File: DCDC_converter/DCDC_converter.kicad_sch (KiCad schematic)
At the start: 30 parts, among them J24 Conn_01x02, U10 MP2491C, U11 AMS1117-3.3, U14 MIC2026-1xM, U15 MIC2026-1xM, U17 MIC2026-1xM, U9 MP2491C

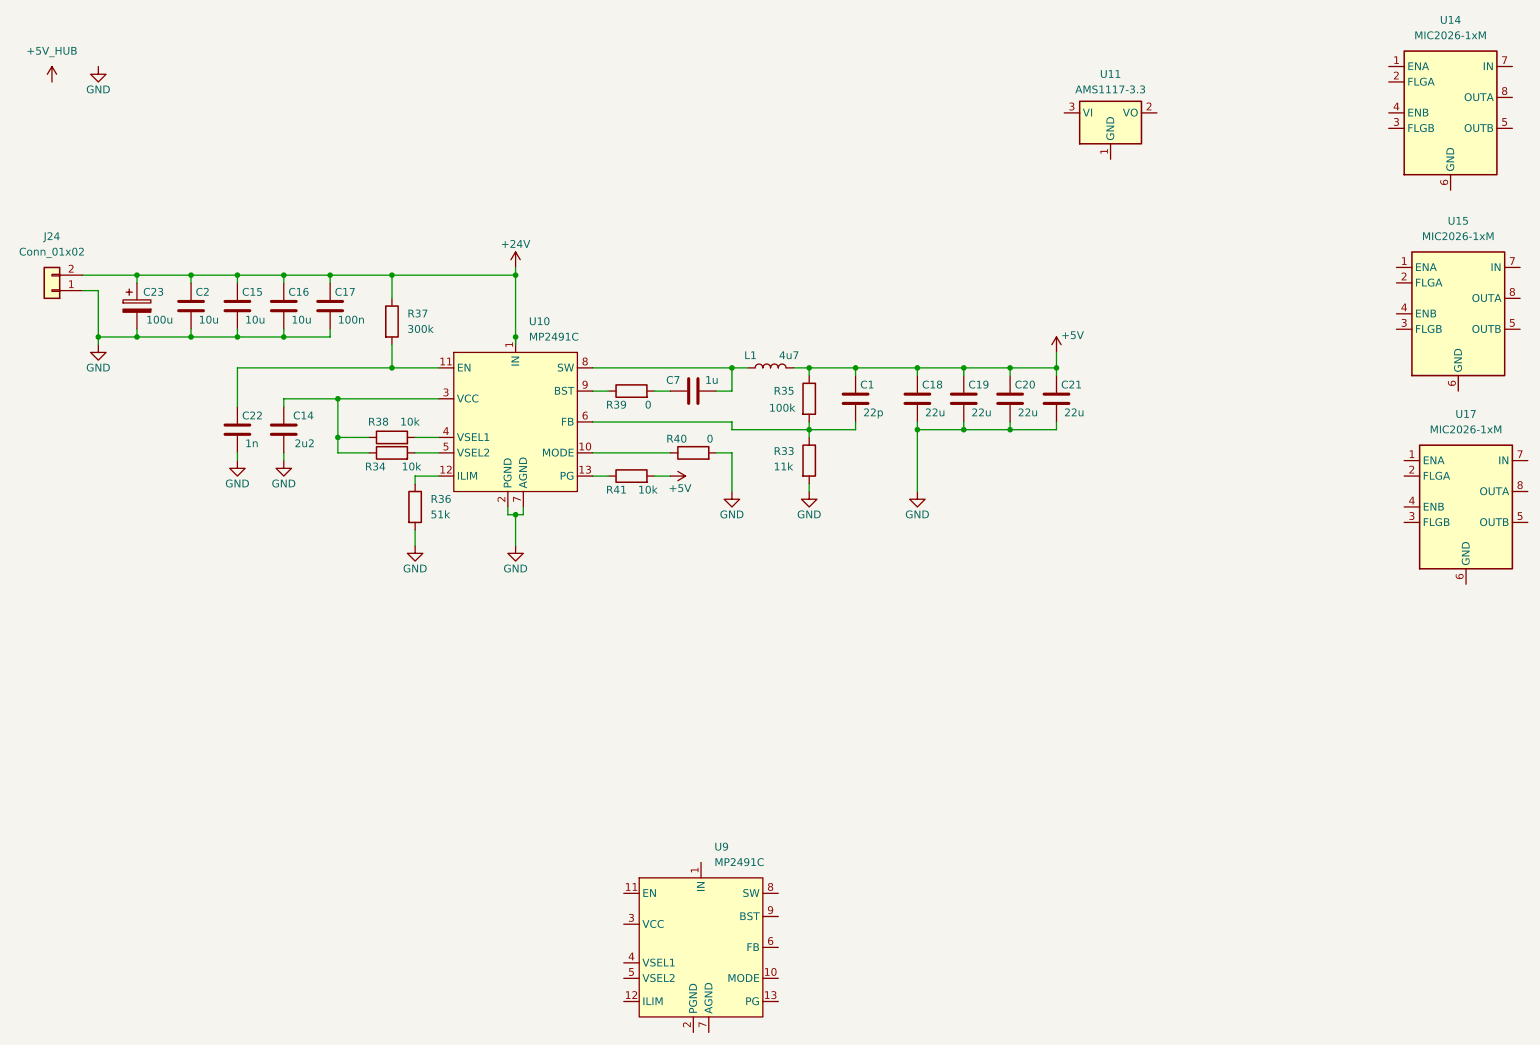
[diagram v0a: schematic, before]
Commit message: Made custom solo PCB for DC/DC converter
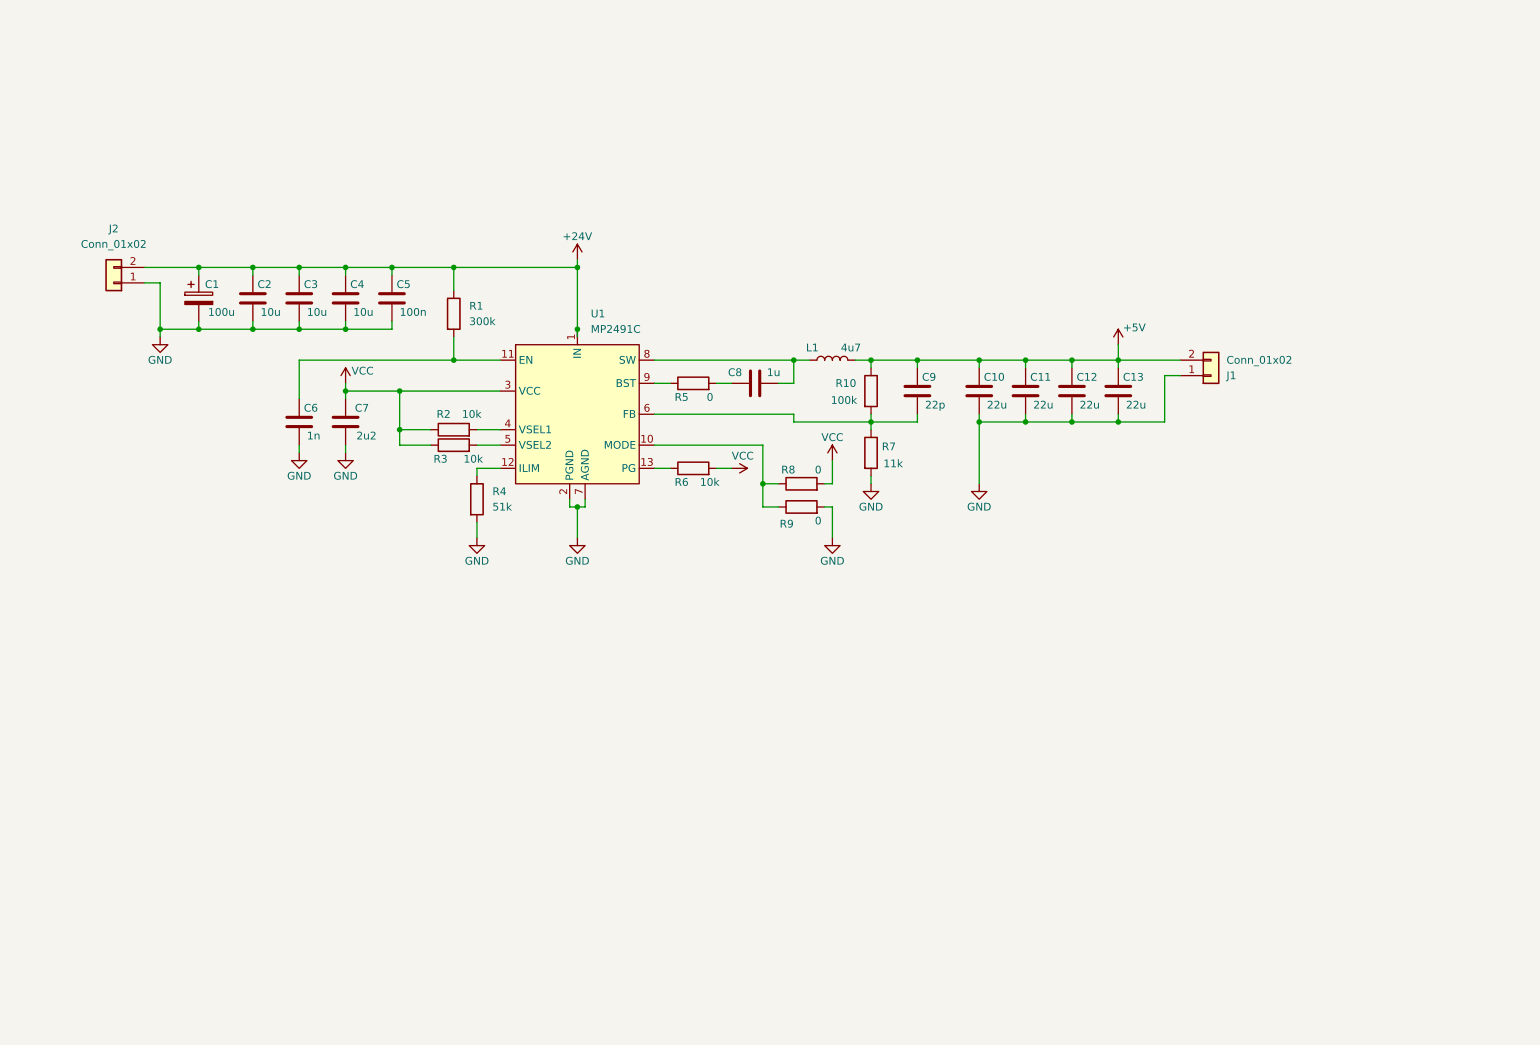
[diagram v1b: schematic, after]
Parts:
- removed C1: 22p, symbol Device:C
- removed C14: 2u2, symbol Device:C
- removed C15, C16: 10u, symbol Device:C
- removed C17: 100n, symbol Device:C
- removed C18, C19, C20, C21: 22u, symbol Device:C
- removed C22: 1n, symbol Device:C
- removed C23: 100u, symbol Device:C_Polarized
- removed J24: Conn_01x02, Connector_Phoenix_MSTB:PhoenixContact_MSTBA_2,5_2-G_1x02_P5.00mm_Horizontal, symbol Connector_Generic:Conn_01x02
- removed R33: 11k, symbol Device:R
- removed R34, R38, R41: 10k, symbol Device:R
- removed R35: 100k, symbol Device:R
- removed R36: 51k, symbol Device:R
- removed R37: 300k, symbol Device:R
- removed R39, R40: 0, symbol Device:R
- removed U10, U9: MP2491C, HK:QFN-13_HK, symbol HK:MP2491C_HK
- removed U11: AMS1117-3.3, Package_TO_SOT_SMD:SOT-223-3_TabPin2, symbol Regulator_Linear:AMS1117-3.3
- removed U14, U15, U17: MIC2026-1xM, Package_SO:SOIC-8_3.9x4.9mm_P1.27mm, symbol Power_Management:MIC2026-1xM
- added C1: 100u, Capacitor_THT:CP_Radial_D6.3mm_P2.50mm, symbol Device:C_Polarized
- added C10, C11, C12, C13: 22u, Capacitor_SMD:C_0805_2012Metric, symbol Device:C
- added C3, C4: 10u, Capacitor_SMD:C_0805_2012Metric, symbol Device:C
- added C5: 100n, Capacitor_SMD:C_0603_1608Metric, symbol Device:C
- added C6: 1n, Capacitor_SMD:C_0603_1608Metric, symbol Device:C
- added C8: 1u, Capacitor_SMD:C_0603_1608Metric, symbol Device:C
- added C9: 22p, Capacitor_SMD:C_0603_1608Metric, symbol Device:C
- added J1, J2: Conn_01x02, Connector_Phoenix_MSTB:PhoenixContact_MSTBA_2,5_2-G_1x02_P5.00mm_Horizontal, symbol Connector_Generic:Conn_01x02
- added R1: 300k, Resistor_SMD:R_0603_1608Metric, symbol Device:R
- added R10: 100k, Resistor_SMD:R_0603_1608Metric, symbol Device:R
- added R2, R3, R6: 10k, Resistor_SMD:R_0603_1608Metric, symbol Device:R
- added R4: 51k, Resistor_SMD:R_0603_1608Metric, symbol Device:R
- added R5, R8, R9: 0, Resistor_SMD:R_0603_1608Metric, symbol Device:R
- added R7: 11k, Resistor_SMD:R_0603_1608Metric, symbol Device:R
- added U1: MP2491C, HK:QFN-13_HK, symbol HK:MP2491C_HK
- C2: footprint (none) -> Capacitor_SMD:C_0805_2012Metric
- C7: value 1u -> 2u2; footprint (none) -> Capacitor_SMD:C_0603_1608Metric
- L1: footprint (none) -> Inductor_SMD:L_Bourns-SRN8040_8x8.15mm
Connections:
- net +24V: now also C1.1, C3.1, C4.1, C5.1, J2.2 (Pin_2), R1.1, U1.1 (IN)
- net +5V: now also C10.1, C11.1, C12.1, C13.1, C9.1, J1.2 (Pin_2), R10.1
- net GND: now also C7.2, C1.2, C10.2, C11.2, C12.2, C13.2, C3.2, C4.2, C5.2, C6.2, J1.1 (Pin_1), J2.1 (Pin_1), R4.2, R7.2, R9.2, U1.2 (PGND), U1.7 (AGND)
- net at L1.1: now also C8.1, U1.8 (SW); no longer C7.1
- new net: R8.1, R9.1, U1.10 (MODE)
- new net: R2.2, U1.4 (VSEL1)
- new net: R4.1, U1.12 (ILIM)
- new net: C9.2, R10.2, R7.1, U1.6 (FB)
- new net: C6.1, R1.2, U1.11 (EN)
- new net: R6.1, U1.13 (PG)
- new net: R3.2, U1.5 (VSEL2)
- new net: R5.1, U1.9 (BST)
- new net: C8.2, R5.2
- new net VCC: C7.1, R2.1, R3.1, R6.2, R8.2, U1.3 (VCC)

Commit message: Last update
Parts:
- added D1: LED, symbol Device:LED
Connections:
- net +24V: now also J2.1 (Pin_1); no longer J2.2 (Pin_2)
- net GND: now also J2.2 (Pin_2); no longer J2.1 (Pin_1)
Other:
- moved on the sheet: J2
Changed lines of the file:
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@@
 	(wire
 		(pts
-			(xy 118.11 58.42) (xy 118.11 59.69)
+			(xy 118.11 57.15) (xy 118.11 59.69)
 		)
 		(stroke
@@
 	(symbol
 		(lib_id "Connector_Generic:Conn_01x02")
-		(at 41.91 62.23 180)
+		(at 41.91 59.69 0)
+		(mirror y)
 		(unit 1)
 		(exclude_from_sim no)
@@
 		(on_board yes)
 		(dnp no)
-		(fields_autoplaced yes)
 		(property "Reference" "J2"
-			(at 41.91 53.34 0)
+			(at 41.91 68.58 0)
 			(effects
 				(font
@@
 		)
 		(property "Value" "Conn_01x02"
-			(at 41.91 55.88 0)
+			(at 41.91 66.04 0)
 			(effects
 				(font
@@
 		)
 		(property "Footprint" "Connector_Phoenix_MSTB:PhoenixContact_MSTBA_2,5_2-G_1x02_P5.00mm_Horizontal"
-			(at 41.91 62.23 0)
+			(at 41.91 59.69 0)
 			(effects
 				(font
@@
 		)
 		(property "Datasheet" "~"
-			(at 41.91 62.23 0)
+			(at 41.91 59.69 0)
 			(effects
 				(font
@@
 		)
 		(property "Description" "Generic connector, single row, 01x02, script generated (kicad-library-utils/schlib/autogen/connector/)"
-			(at 41.91 62.23 0)
+			(at 41.91 59.69 0)
 			(effects
 				(font
@@
 	)
 	(symbol
+		(lib_id "Device:LED")
+		(at 139.7 105.41 90)
+		(unit 1)
+		(exclude_from_sim no)
+		(in_bom yes)
+		(on_board yes)
+		(dnp no)
+		(fields_autoplaced yes)
+		(property "Reference" "D1"
+			(at 143.51 105.7274 90)
+			(effects
+				(font
+					(size 1.27 1.27)
+				)
+				(justify right)
+			)
+		)
+		(property "Value" "LED"
+			(at 143.51 108.2674 90)
+			(effects
+				(font
+					(size 1.27 1.27)
+				)
+				(justify right)
+			)
+		)
+		(property "Footprint" ""
+			(at 139.7 105.41 0)
+			(effects
+				(font
+					(size 1.27 1.27)
+				)
+				(hide yes)
+			)
+		)
+		(property "Datasheet" "~"
+			(at 139.7 105.41 0)
+			(effects
+				(font
+					(size 1.27 1.27)
+				)
+				(hide yes)
+			)
+		)
+		(property "Description" "Light emitting diode"
+			(at 139.7 105.41 0)
+			(effects
+				(font
+					(size 1.27 1.27)
+				)
+				(hide yes)
+			)
+		)
+		(pin "2"
+		)
+		(pin "1"
+		)
+		(instances
+			(project ""
+				(path "/ace81164-188f-43a4-8ebe-64248f08801c"
+					(reference "D1")
+					(unit 1)
+				)
+			)
+		)
+	)
+	(symbol
 		(lib_id "Device:R")
 		(at 97.79 67.31 0)
@@
 	(symbol
 		(lib_id "power:+24V")
-		(at 118.11 58.42 0)
+		(at 118.11 57.15 0)
 		(unit 1)
 		(exclude_from_sim no)
@@
 		(dnp no)
 		(property "Reference" "#PWR0110"
-			(at 118.11 62.23 0)
+			(at 118.11 60.96 0)
 			(effects
 				(font
@@
 		)
 		(property "Value" "+24V"
-			(at 118.11 54.61 0)
+			(at 118.11 53.34 0)
 			(effects
 				(font
@@
 		)
 		(property "Footprint" ""
-			(at 118.11 58.42 0)
+			(at 118.11 57.15 0)
 			(effects
 				(font
@@
 		)
 		(property "Datasheet" ""
-			(at 118.11 58.42 0)
+			(at 118.11 57.15 0)
 			(effects
 				(font
@@
 		)
 		(property "Description" "Power symbol creates a global label with name \"+24V\""
-			(at 118.11 58.42 0)
+			(at 118.11 57.15 0)
 			(effects
 				(font

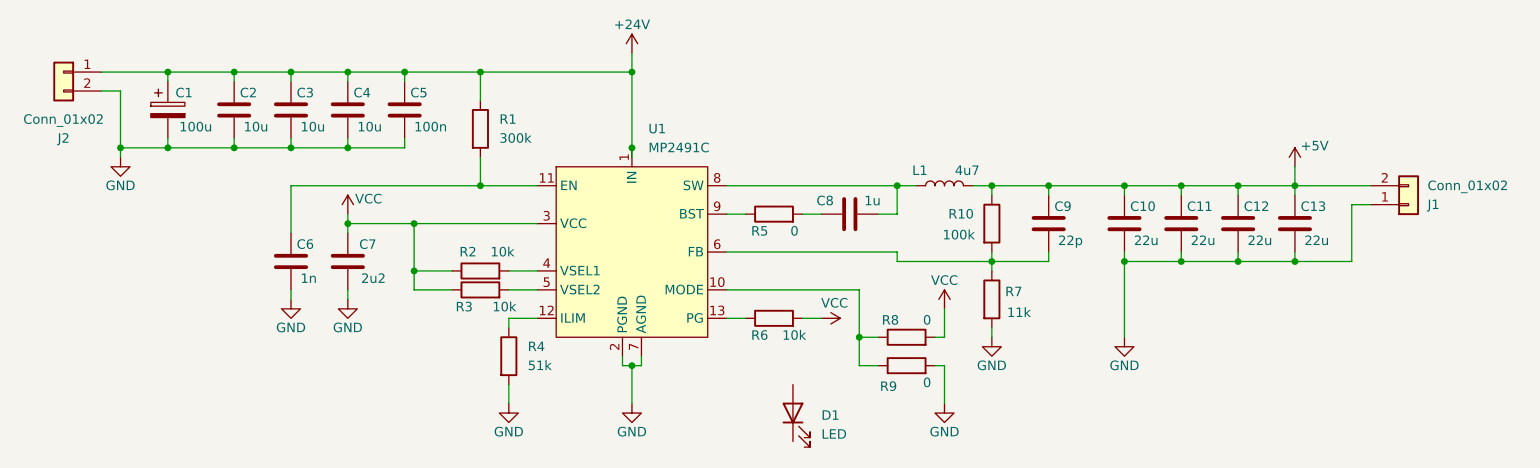
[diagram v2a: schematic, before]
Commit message: Adjusting the size of the PCB
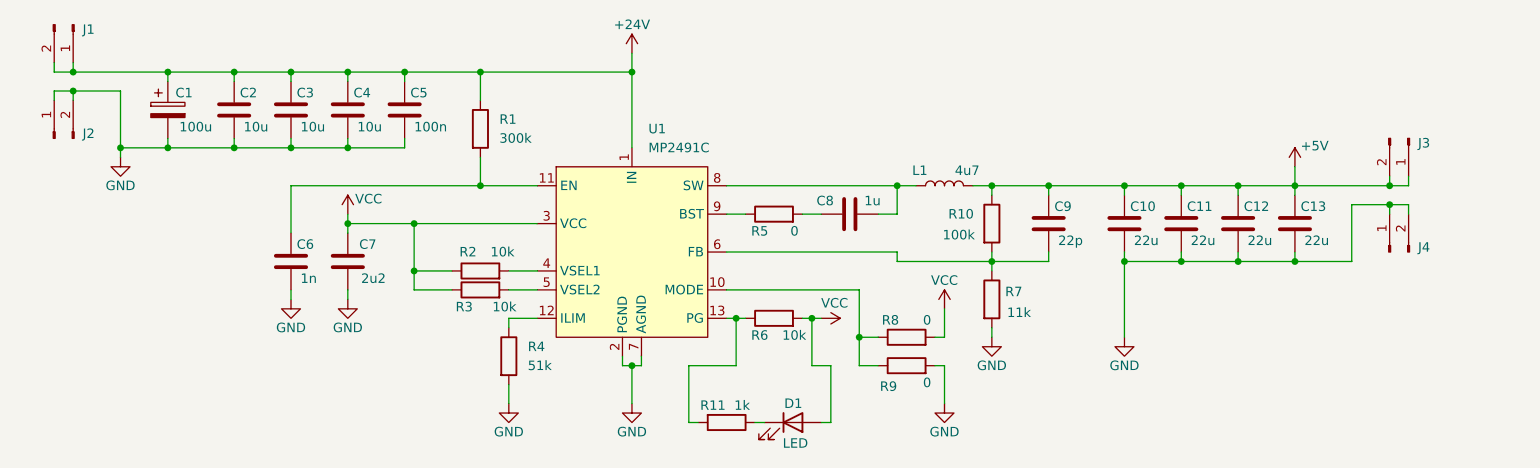
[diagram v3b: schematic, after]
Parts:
- removed J1, J2: Conn_01x02, Connector_Phoenix_MSTB:PhoenixContact_MSTBA_2,5_2-G_1x02_P5.00mm_Horizontal, symbol Connector_Generic:Conn_01x02
- added J1, J2, J3, J4: Conn_01x02_Pin, Connector_PinHeader_2.54mm:PinHeader_1x02_P2.54mm_Vertical, symbol Connector:Conn_01x02_Pin
- added R11: 1k, Resistor_SMD:R_0603_1608Metric, symbol Device:R
- D1: footprint (none) -> LED_SMD:LED_0603_1608Metric
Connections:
- net +24V: now also J1.1 (Pin_1), J1.2 (Pin_2)
- net +5V: now also J3.1 (Pin_1), J3.2 (Pin_2)
- net GND: now also J2.1 (Pin_1), J2.2 (Pin_2), J4.1 (Pin_1), J4.2 (Pin_2)
- net VCC: now also D1.2 (A)
- net at R6.1, U1.13 (PG): now also R11.2
- net at D1.1 (K): now also R11.1
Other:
- moved on the sheet: D1
